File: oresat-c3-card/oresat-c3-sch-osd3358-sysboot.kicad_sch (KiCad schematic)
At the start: 23 parts, among them J6 Conn_01x02, U1 OSD3358-1G-ISM, U39 TCAN330

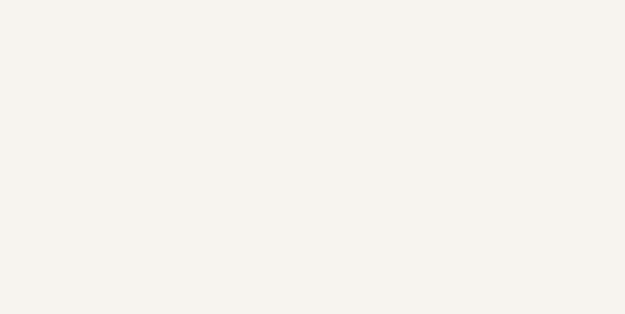
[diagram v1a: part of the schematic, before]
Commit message: schematic changes following design review
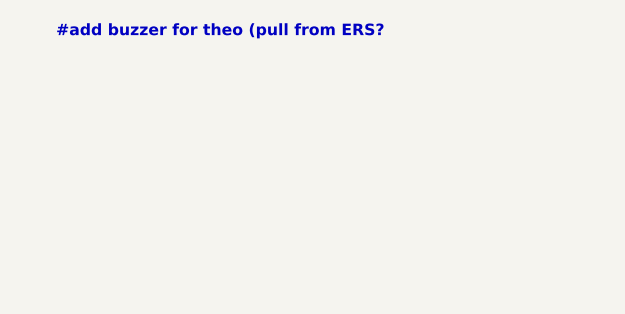
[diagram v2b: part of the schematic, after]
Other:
- note added: "#add buzzer for theo (pull from ERS?"
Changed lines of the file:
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@@
+		)
+	)
+	(text "#add buzzer for theo (pull from ERS?"
+		(exclude_from_sim no)
+		(at 47.752 27.686 0)
+		(effects
+			(font
+				(size 1.27 1.27)
+				(thickness 0.254)
+				(bold yes)
+			)
 		)
 	)

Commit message: Design review on power and RF
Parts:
- U1: Distributor (none) -> DigiKey; MPN OSD3358-1G-ISM -> OSD3358-512M-BSM
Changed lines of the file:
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@@
 			)
 		)
-		(property "Description" "Embedded Module ARM® Cortex®-A8, AM3358 1GHz 1GB"
+		(property "Description" "OSD335x Embedded Module 1GHz 512MB"
 			(at 147.32 53.34 0)
 			(effects
@@
 			)
 		)
-		(property "MPN" "OSD3358-1G-ISM"
+		(property "MPN" "OSD3358-512M-BSM"
 			(at 147.32 58.42 0)
 			(effects
@@
 			(effects
 				(font
+					(size 1.27 1.27)
+				)
+				(hide yes)
+			)
+		)
+		(property "Distributor" "DigiKey"
+			(at 147.32 55.88 0)
+			(effects
+				(font

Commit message: Updating BOM and switching to oresat-passive footprints. Fixed some power cutoff limits, and fixed another DC voltage leverl on an LNA!
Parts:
- C56, R72, R73, R74, U1, U39: DST Digi-Key -> DigiKey
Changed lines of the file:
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@@
 			)
 		)
-		(property "DST" "Digi-Key"
+		(property "DST" "DigiKey"
 			(at 256.54 185.42 0)
 			(effects
@@
 			)
 		)
-		(property "DST" "Digi-Key"
+		(property "DST" "DigiKey"
 			(at 132.08 90.17 0)
 			(effects
@@
 			)
 		)
-		(property "DST" "Digi-Key"
+		(property "DST" "DigiKey"
 			(at 116.84 74.93 0)
 			(effects
@@
 			)
 		)
-		(property "Datasheet" ""
+		(property "Datasheet" "https://octavosystems.com/docs/osd335x-sm-datasheet/"
 			(at 147.32 157.48 0)
 			(effects
@@
 			)
 		)
-		(property "DST" "Digi-Key"
+		(property "DST" "DigiKey"
 			(at 147.32 157.48 0)
 			(effects
@@
 			)
 		)
-		(property "DST" "Digi-Key"
+		(property "DST" "DigiKey"
 			(at 231.14 185.42 0)
 			(effects
@@
 			)
 		)
-		(property "DST" "Digi-Key"
+		(property "DST" "DigiKey"
 			(at 213.36 107.95 0)
 			(effects

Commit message: All footprints updated. Passes ERC/DRC.
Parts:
- C56: footprint Capacitor_SMD:C_0603_1608Metric -> oresat-passives:0603-C-NOSILK; DPN 587-3472-1-ND -> 399-6856-1-ND; MFR Taiyo Yuden -> KEMET; MPN TMK107BJ104KAHT -> C0603C104K5RACAUTO
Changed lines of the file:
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@@
 			)
 		)
-		(property "Footprint" "Capacitor_SMD:C_0603_1608Metric"
+		(property "Footprint" "oresat-passives:0603-C-NOSILK"
 			(at 116.84 74.93 0)
 			(effects
@@
 			)
 		)
-		(property "Datasheet" "~"
+		(property "Datasheet" "https://search.kemet.com/download/specsheet/C0603C104K5RACAUTO"
 			(at 116.84 74.93 0)
 			(effects
@@
 			)
 		)
-		(property "Description" "100 nF (0.1µF) ±10% 25V Ceramic Capacitor X5R 0603 (1608 Metric)"
+		(property "Description" "0.1 µF ±10% 50V Ceramic Capacitor X7R 0603 (1608 Metric)"
 			(at 116.84 74.93 0)
 			(effects
@@
 			)
 		)
-		(property "DPN" "587-3472-1-ND"
+		(property "DPN" "399-6856-1-ND"
 			(at 116.84 74.93 0)
 			(effects
@@
 			)
 		)
-		(property "MFR" "Taiyo Yuden"
+		(property "MFR" "KEMET"
 			(at 116.84 74.93 0)
 			(effects
@@
 			)
 		)
-		(property "MPN" "TMK107BJ104KAHT"
+		(property "MPN" "C0603C104K5RACAUTO"
 			(at 116.84 74.93 0)
 			(effects

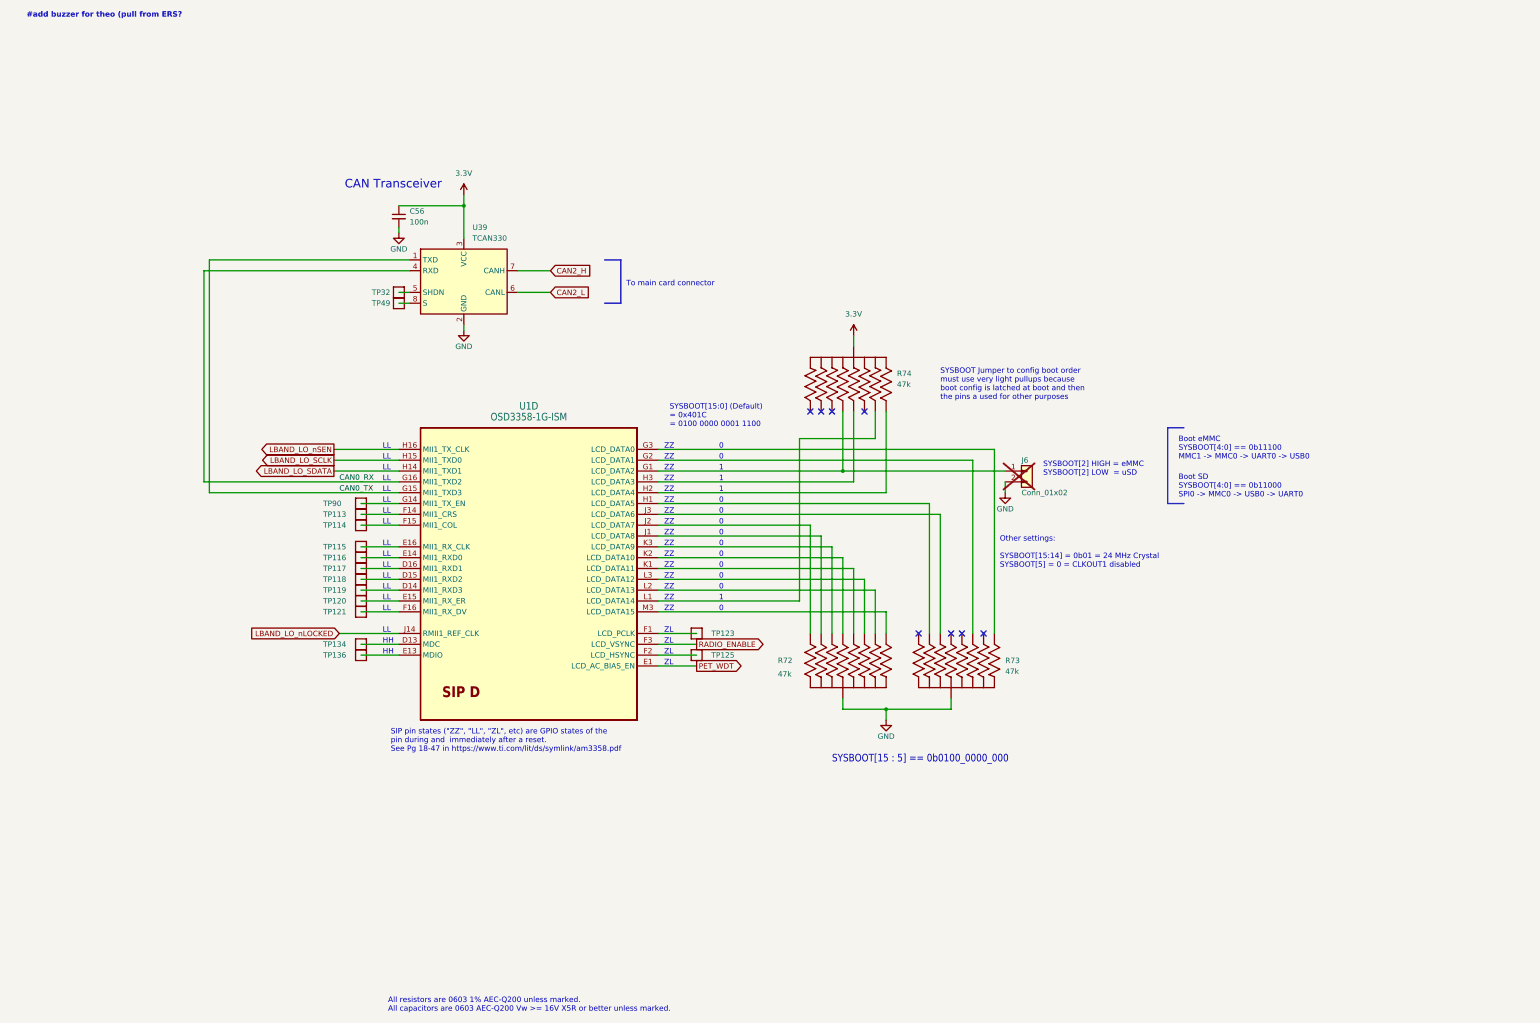
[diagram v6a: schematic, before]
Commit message: Last minute fixes.
Added Theo's space buzzer. Added important kaomoji message. Fixed Makefile so that it ignores
bad VRML footprints. Successfully builds!
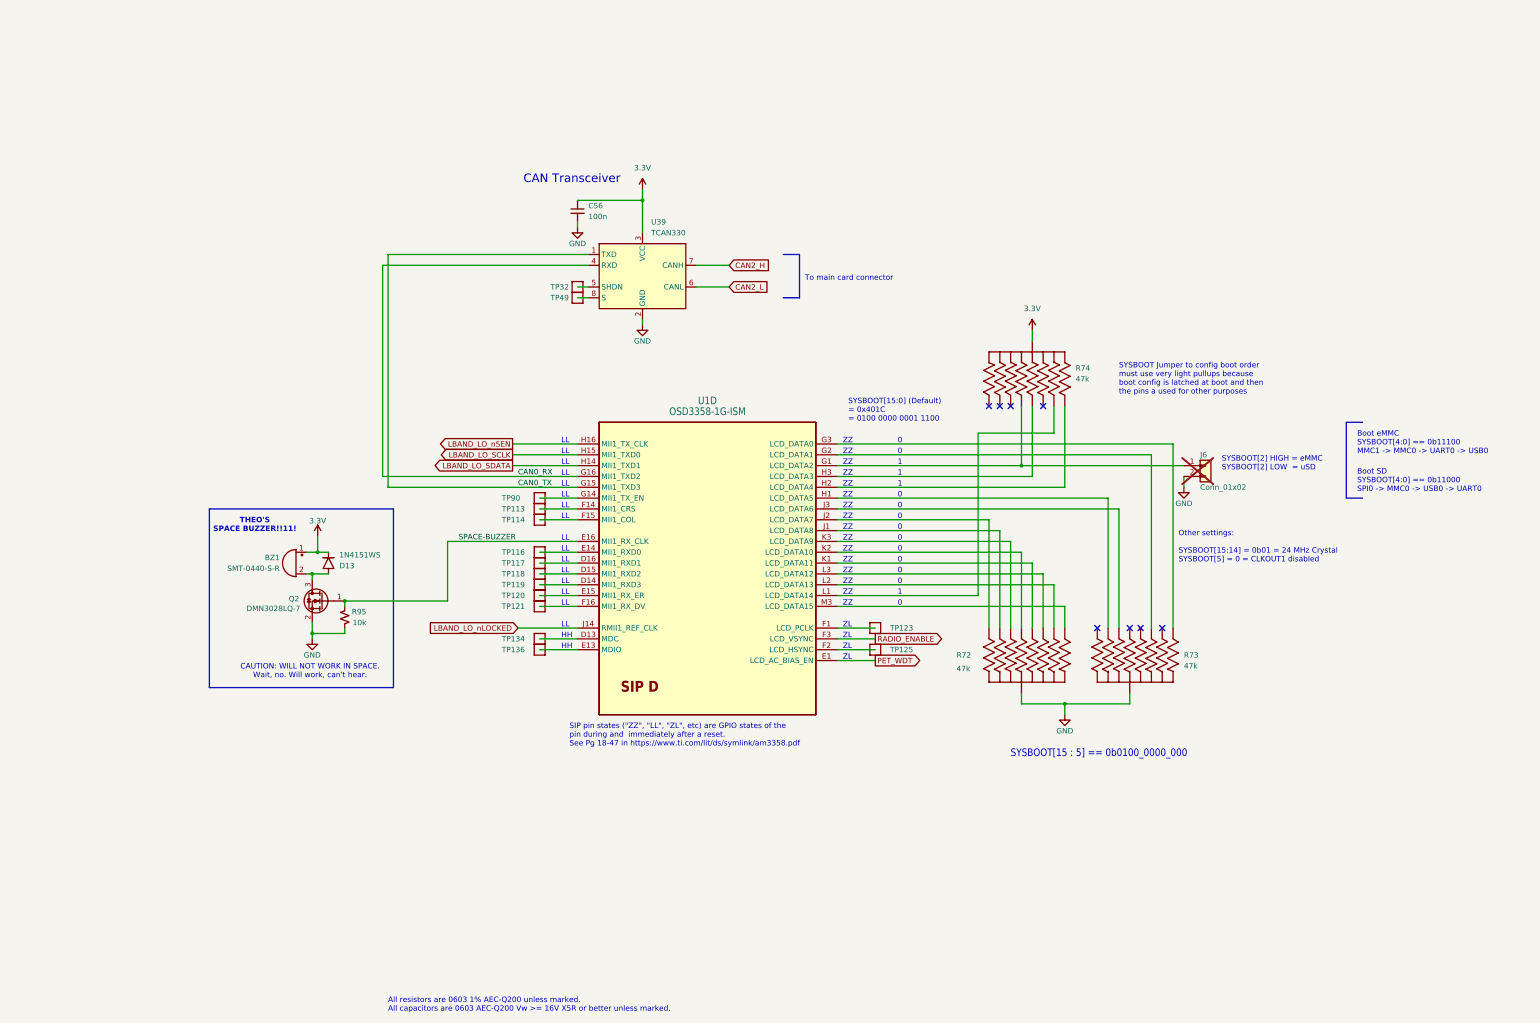
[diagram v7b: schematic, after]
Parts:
- removed TP115: Test-Point, oresat-misc:TestPoint_Pad_D1.0mm, symbol oresat-misc:Test-Point-1mm-round
- added BZ1: SMT-0440-S-R, oresat-misc:SMT-0440-S-R, symbol Device:Buzzer
- added D13: 1N4151WS, Diode_SMD:D_SOD-323, symbol oresat-diodes:1N4151WS-HE3
- added Q2: DMN3028LQ-7, Package_TO_SOT_SMD:SOT-23-3, symbol Transistor_FET:Q_NMOS_GSD
- added R95: 10k, oresat-passives:0603-C-NOSILK, symbol Device:R_Small_US
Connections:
- net 3.3V: now also BZ1.1 (+), D13.1
- net GND: now also Q2.2 (S), R95.2
- net SPACE-BUZZER: now reaches U1.E16 (MII1_RX_CLK)
- net SPACE-BUZZER: now also Q2.1 (G), R95.1
- new net: BZ1.2 (-), D13.2, Q2.3 (D)
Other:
- note added: "CAUTION: WILL NOT WORK IN SPACE. Wait, no. Will work, can't hear."
- note added: "THEO'S SPACE BUZZER!!11!"
- note removed: "#add buzzer for theo (pull from ERS?"
- moved on the sheet: C56, J6, R72, R73, R74, TP113, TP114, TP116, TP117, TP118, TP119, TP120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

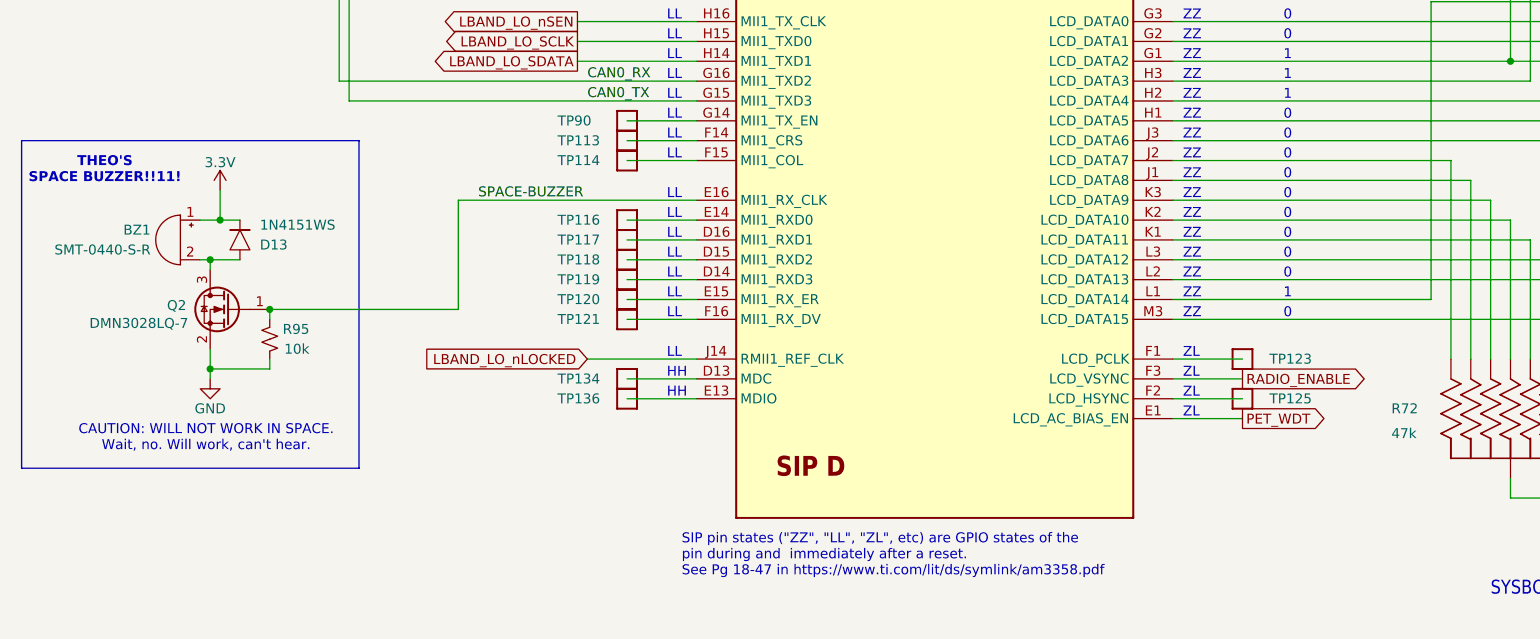
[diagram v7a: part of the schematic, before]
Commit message: Minor polishing on schematic, mostly text notes.
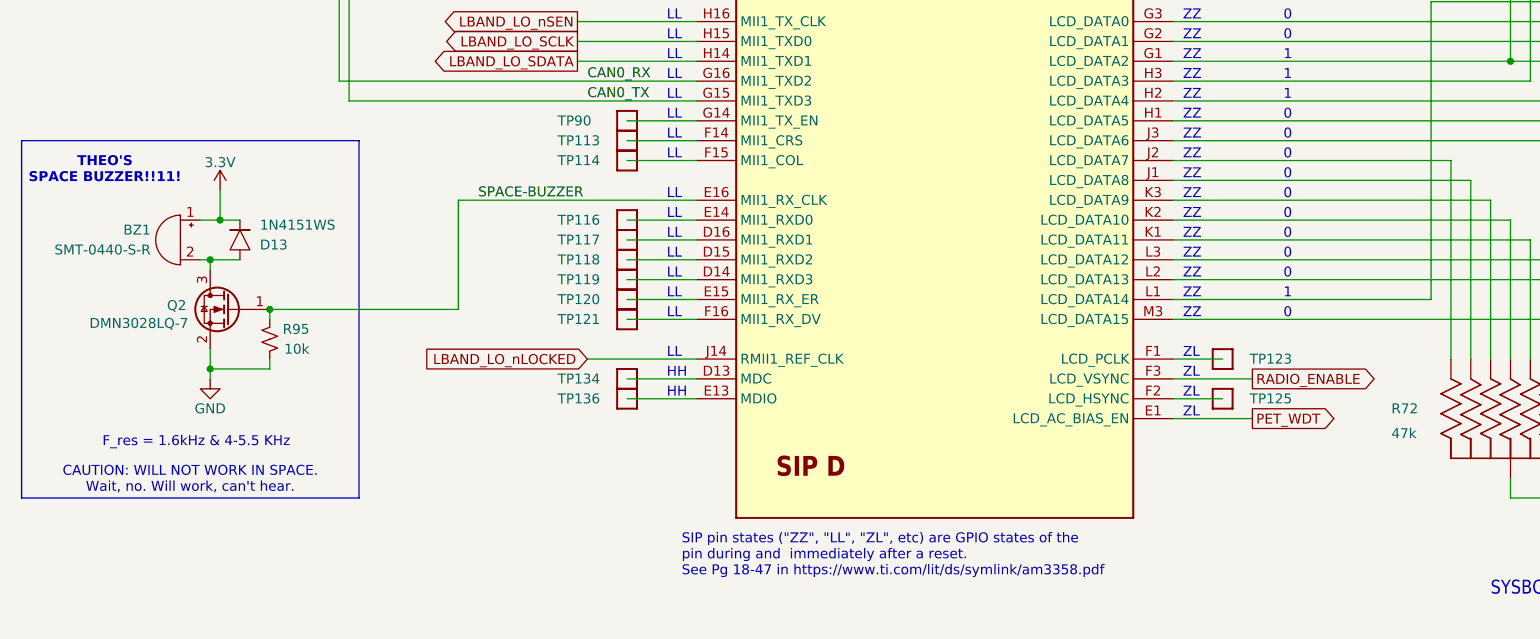
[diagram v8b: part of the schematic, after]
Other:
- note added: "F_res = 1.6kHz & 4-5.5 KHz"
- moved on the sheet: TP123, TP125
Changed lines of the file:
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@@
 	(rectangle
 		(start 72.39 143.51)
-		(end 115.57 185.42)
+		(end 115.57 189.23)
 		(stroke
 			(width 0)
@@
 		)
 	)
+	(text "F_res = 1.6kHz & 4-5.5 KHz"
+		(exclude_from_sim no)
+		(at 94.742 182.118 0)
+		(effects
+			(font
+				(size 1.27 1.27)
+			)
+		)
+	)
 	(text "Other settings:\n\nSYSBOOT[15:14] = 0b01 = 24 MHz Crystal\nSYSBOOT[5] = 0 = CLKOUT1 disabled"
 		(exclude_from_sim no)
@@
 	(text "CAUTION: WILL NOT WORK IN SPACE.\nWait, no. Will work, can't hear."
 		(exclude_from_sim no)
-		(at 96.012 181.61 0)
+		(at 93.98 186.944 0)
 		(effects
 			(font
@@
 	(wire
 		(pts
-			(xy 219.71 179.07) (xy 228.6 179.07)
+			(xy 219.71 179.07) (xy 229.87 179.07)
 		)
 		(stroke
@@
 	(wire
 		(pts
-			(xy 219.71 176.53) (xy 228.6 176.53)
+			(xy 219.71 176.53) (xy 226.06 176.53)
 		)
 		(stroke
@@
 	(wire
 		(pts
-			(xy 219.71 173.99) (xy 228.6 173.99)
+			(xy 219.71 173.99) (xy 229.87 173.99)
 		)
 		(stroke
@@
 	(wire
 		(pts
-			(xy 219.71 171.45) (xy 228.6 171.45)
+			(xy 219.71 171.45) (xy 226.06 171.45)
 		)
 		(stroke
@@
 	(global_label "PET_WDT"
 		(shape output)
-		(at 228.6 179.07 0)
+		(at 229.87 179.07 0)
 		(fields_autoplaced yes)
 		(effects
@@
 		)
 		(property "Intersheetrefs" "${INTERSHEET_REFS}"
-			(at 239.549 179.07 0)
+			(at 240.819 179.07 0)
 			(effects
 				(font
@@
 	(global_label "RADIO_ENABLE"
 		(shape output)
-		(at 228.6 173.99 0)
+		(at 229.87 173.99 0)
 		(fields_autoplaced yes)
 		(effects
@@
 		)
 		(property "Intersheetrefs" "${INTERSHEET_REFS}"
-			(at 245.0525 173.99 0)
+			(at 246.3225 173.99 0)
 			(effects
 				(font
@@
 	(symbol
 		(lib_id "oresat-misc:Test-Point-1mm-round")
-		(at 228.6 171.45 90)
+		(at 226.06 171.45 90)
 		(unit 1)
 		(exclude_from_sim yes)
@@
 		(dnp no)
 		(property "Reference" "TP123"
-			(at 237.49 171.45 90)
+			(at 234.95 171.45 90)
 			(effects
 				(font
@@
 		)
 		(property "Value" "Test-Point"
-			(at 226.06 171.45 0)
+			(at 223.52 171.45 0)
 			(effects
 				(font
@@
 		)
 		(property "Footprint" "oresat-misc:TestPoint_Pad_D1.0mm"
-			(at 218.44 171.45 0)
+			(at 215.9 171.45 0)
 			(effects
 				(font
@@
 		)
 		(property "Datasheet" ""
-			(at 228.6 171.45 0)
+			(at 226.06 171.45 0)
 			(effects
 				(font
@@
 		)
 		(property "Description" "1mm round SMT test point"
-			(at 228.6 171.45 0)
+			(at 226.06 171.45 0)
 			(effects
 				(font
@@
 	(symbol
 		(lib_id "oresat-misc:Test-Point-1mm-round")
-		(at 228.6 176.53 90)
+		(at 226.06 176.53 90)
 		(unit 1)
 		(exclude_from_sim yes)
@@
 		(dnp no)
 		(property "Reference" "TP125"
-			(at 237.49 176.53 90)
+			(at 234.95 176.53 90)
 			(effects
 				(font
@@
 		)
 		(property "Value" "Test-Point"
-			(at 226.06 176.53 0)
+			(at 223.52 176.53 0)
 			(effects
 				(font
@@
 		)
 		(property "Footprint" "oresat-misc:TestPoint_Pad_D1.0mm"
-			(at 218.44 176.53 0)
+			(at 215.9 176.53 0)
 			(effects
 				(font
@@
 		)
 		(property "Datasheet" ""
-			(at 228.6 176.53 0)
+			(at 226.06 176.53 0)
 			(effects
 				(font
@@
 		)
 		(property "Description" "1mm round SMT test point"
-			(at 228.6 176.53 0)
+			(at 226.06 176.53 0)
 			(effects
 				(font
